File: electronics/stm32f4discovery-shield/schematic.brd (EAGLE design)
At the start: 135.6 x 110.5 mm, 41 parts, among them IC1 MAX3468CPA, IC3 LM340H-12, IC4 LM340H-12, J1 POWER_JACKSLT, Q1 BC548

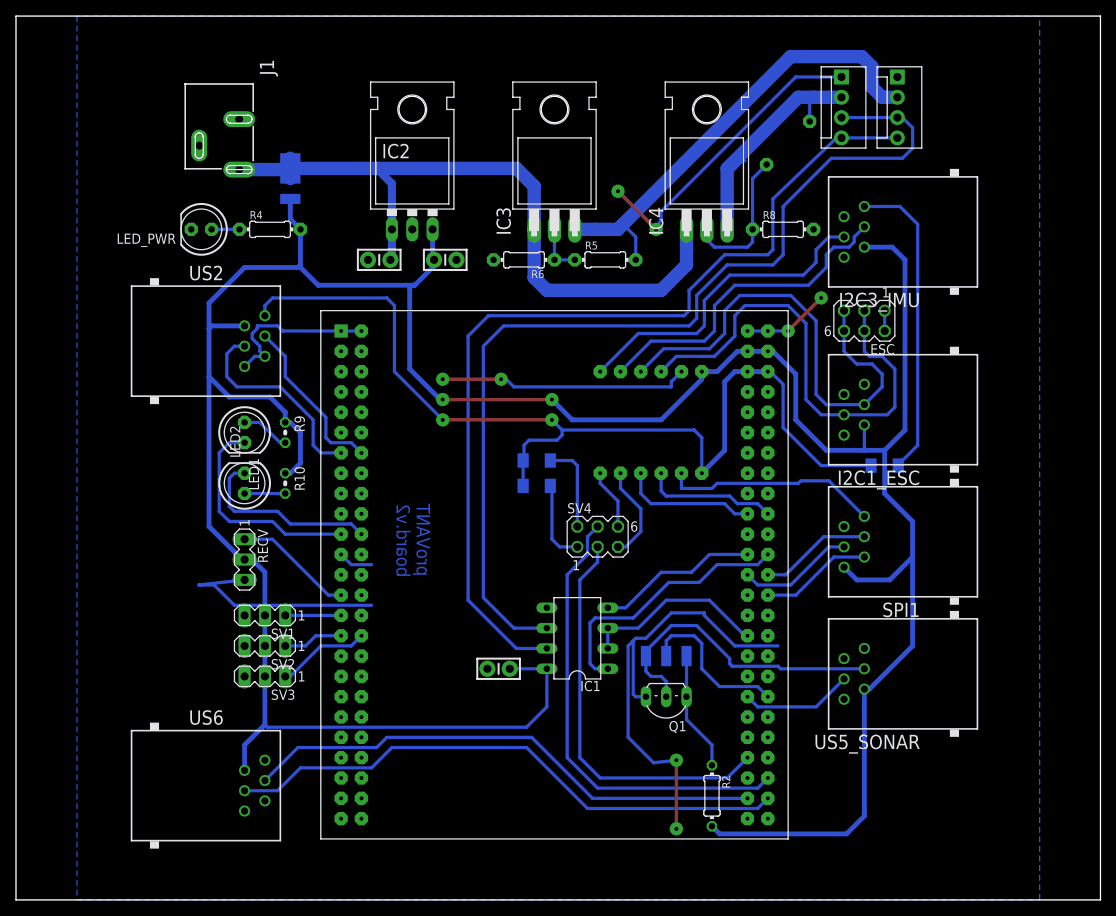
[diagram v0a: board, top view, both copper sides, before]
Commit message: Adicionado o jack para sensores analógicos. LEDs trocados para LEDs de 3mm. Verificaçao de routing do GND feita - aparentemente, sem problemas.
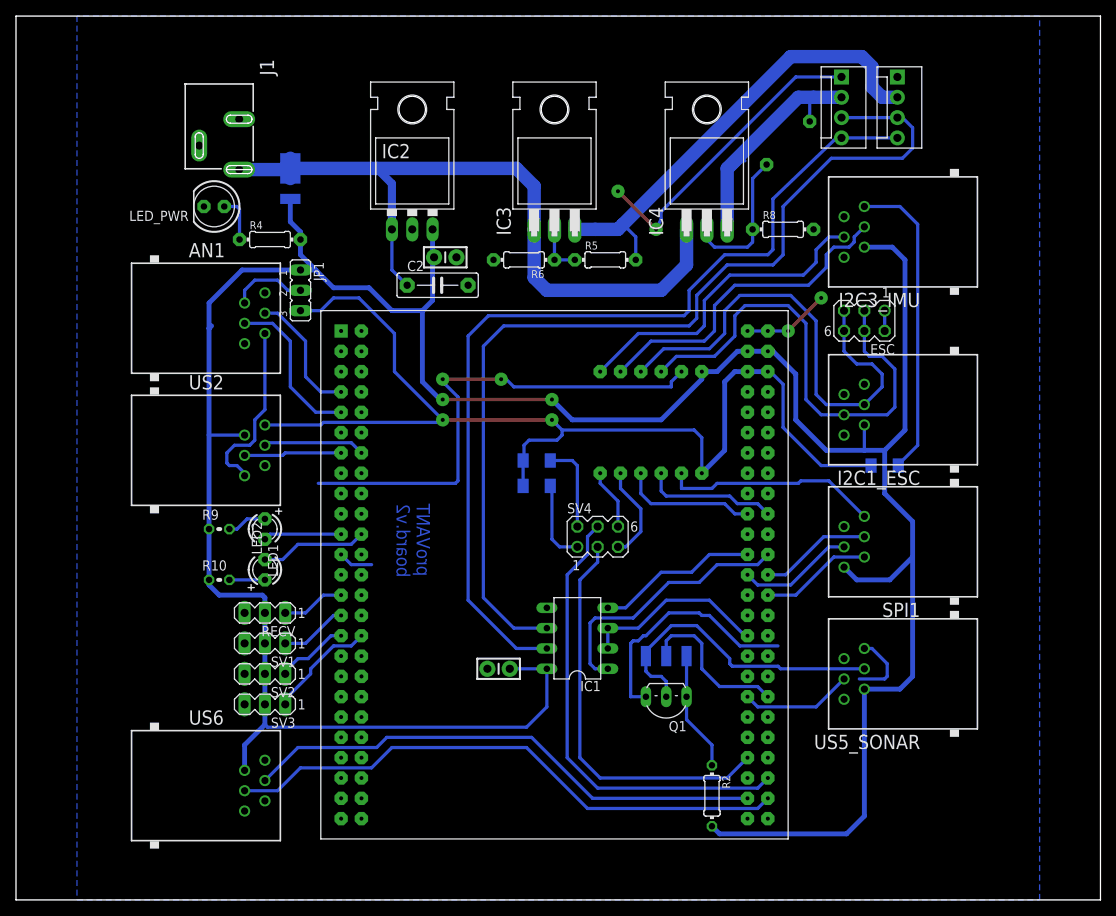
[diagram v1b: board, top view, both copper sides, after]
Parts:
- added AN1: RJ11-2L-B, con-tycoelectronics:RJ11-NO_SHIELD
- added JP1: (no value), jumper:JP2
- C2: device SparkFun-Capacitors:CAP-PTH-SMALL-KIT -> capacitor-wima:C7.5B3
- LED1, LED2: device adafruit:LED5MM -> adafruit:LED3MM
- moved R9 14.6 mm to (8.89, 46.4), turned to 0 degrees
- moved R10 14.6 mm to (8.89, 40.0), turned to 0 degrees
- moved US2 13.7 mm to (5.71, 56.2)
- moved LED1 12.3 mm to (14.6, 46.4)
- moved LED2 11.1 mm to (14.6, 41.3)
- moved C2 7.96 mm to (36.2, 76.8), turned to 0 degrees
- moved RECV 7.13 mm to (14.6, 35.9), turned to 180 degrees
- moved SV1 3.49 mm to (14.6, 32.1)
- moved SV2 3.49 mm to (14.6, 28.3)
- moved SV3 3.49 mm to (14.6, 24.4)
- moved LED_PWR 3.27 mm to (8.26, 86.7)
- moved R4 1.27 mm to (15.2, 82.5)
- moved C3 0.32 mm to (37.1, 80.3)
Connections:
- new net ADC1: AN1.3, U$1.P$7
- new net ADC3: AN1.4, U$1.P$9
- new net N$10: AN1.2, JP1.2
- net 3.3V: now also JP1.3
- net 5V: now also JP1.1
- net GND: now also AN1.5, AN1.6
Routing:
- net ADC3: track 0.00 -> 20.0 mm
- net PB1/PWM: track 27.4 -> 9.79 mm
- net ADC1: track 0.00 -> 16.2 mm
- net 3.3V: track 123.3 -> 138.3 mm
- net GND: track 222.4 -> 207.5 mm, vias 8 -> 6
- net 5V: track 380.4 -> 365.8 mm
- net PA3/USART2_RX: track 25.6 -> 12.2 mm
- net PB0/PWM: track 23.6 -> 13.4 mm
- net N$10: track 0.00 -> 9.62 mm
- net PA2/USART2_TX: track 21.1 -> 12.7 mm
- net PE9/PWM: track 15.0 -> 7.91 mm
- net VCC: track 90.7 -> 94.6 mm
- net N$4: track 3.49 -> 5.85 mm
- net PE14/PWM: track 11.6 -> 13.8 mm
- net PE13/PWM: track 7.51 -> 9.14 mm
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
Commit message: Realizado o roteamento Dual-Layer para fresamento.
Aumento de espacamento (trilhas de 24mil, espacamento 24mil)
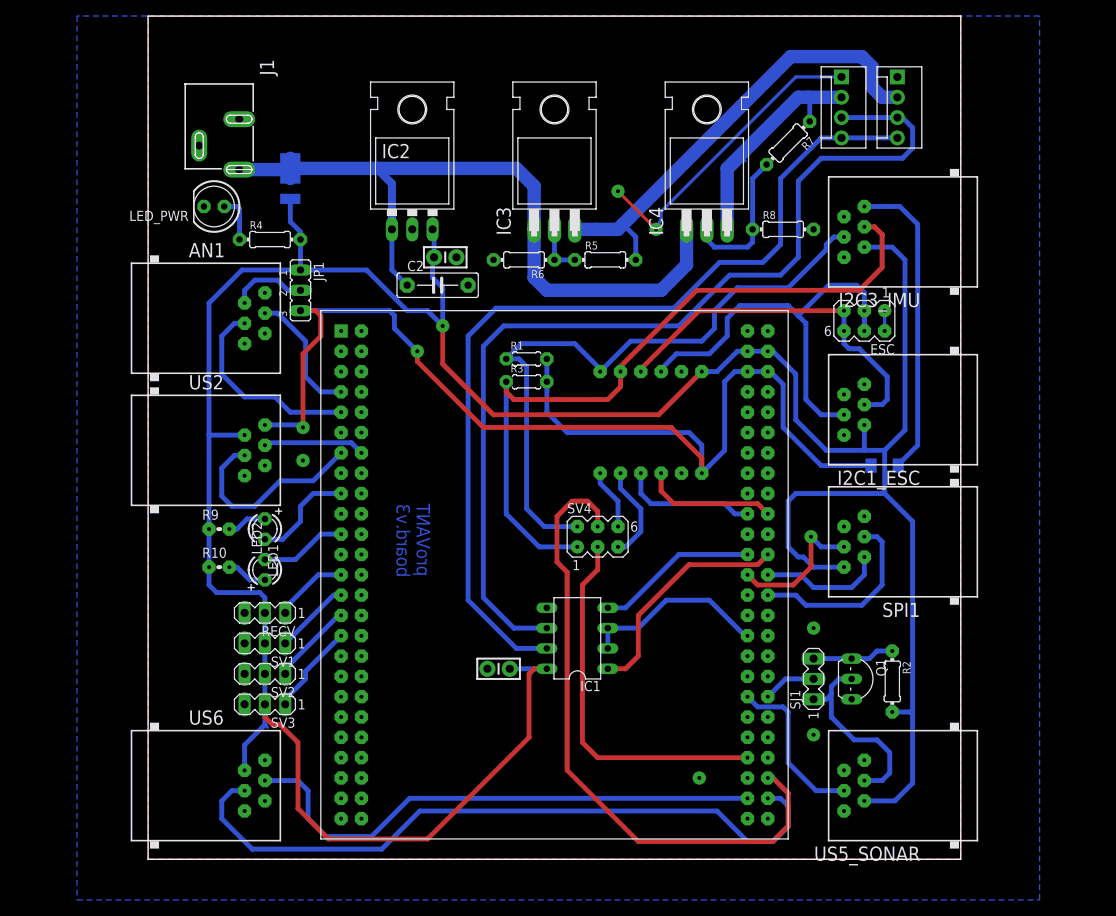
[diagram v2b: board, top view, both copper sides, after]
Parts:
- R1, R3: device adafruit:M1406 -> adafruit:0204/5
- R10, R9: device adafruit:0204V -> rcl:0204V
- SJ1: device jumper:SJ_2W -> con-lstb:MA03-1
- moved R2 26.7 mm to (93.0, 27.3)
- moved Q1 24.7 mm to (89.2, 27.6), turned to 270 degrees
- moved SJ1 18.6 mm to (83.2, 27.6), flipped to the top, turned to 90 degrees
- moved US5_SONAR 14.0 mm to (95.9, 14.3)
- moved R3 13.1 mm to (47.3, 64.8), flipped to the top
- moved R1 12.8 mm to (47.3, 67.6), flipped to the top
- moved R10 1.59 mm to (8.89, 41.6)
- flipped R7 to the top, turned to 225 degrees
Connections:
- new net PA7/PWM: LED1.K, U$1.P$17
- new net PE7: RECV.1, U$1.P$25
- net PB0/PWM: no longer LED2.K
- net PB1/PWM: now also LED2.K; no longer LED1.K
- net PB3/SPI1_SCK: now also SPI1.4; no longer SPI1.2
- net PB5/SPI1_MOSI: now also SPI1.2; no longer SPI1.4
- net PE11/PWM: now also SV2.1; no longer SV1.1
- net PE13/PWM: now also SV3.1; no longer SV2.1
- net PE14/PWM: no longer SV3.1
- net PE9/PWM: now also SV1.1; no longer RECV.1
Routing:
- net GND: track 207.5 -> 41.2 mm
- net SCL2: track 51.5 -> 90.8 mm
- net SDA2: track 52.1 -> 81.3 mm
- net PC9/I2C3_SDA: track 57.7 -> 80.1 mm
- net PC7/USART6_RX: track 71.3 -> 87.8 mm
- net 3.3V: track 138.3 -> 154.7 mm
- net SCL1: track 60.4 -> 46.0 mm
- net SONAR_RX: track 38.7 -> 24.5 mm
- net 5V: track 365.8 -> 379.7 mm, vias 2 -> 1
- net PE14/PWM: track 13.8 -> 0.00 mm
- net PB0/PWM: track 13.4 -> 0.00 mm
- net PC11/USART3_RX: track 19.9 -> 6.64 mm
- net PA3/USART2_RX: track 12.2 -> 25.2 mm
- net PA7/PWM: track 0.00 -> 13.0 mm
- net PB3/SPI1_SCK: track 14.0 -> 23.7 mm
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- added copper zone on layer 1, net GND
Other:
- board size 135.6 x 110.5 mm -> 101.6 x 105.4 mm
- board text added: "proVANT board.v3"
- board text removed: "proVANT board.v2"

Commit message: Small fixes.
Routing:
- net PC6/USART6_TX: track 67.2 -> 64.4 mm
- net ADC1: track 16.2 -> 14.0 mm
- net 5V: track 379.7 -> 377.6 mm
- net PB3/SPI1_SCK: track 23.7 -> 22.5 mm
- net SDA1: track 56.5 -> 55.3 mm
- net PB5/SPI1_MOSI: track 15.6 -> 14.3 mm
- net N$10: track 9.62 -> 8.35 mm
- net PA3/USART2_RX: track 25.2 -> 26.3 mm
- net PC7/USART6_RX: track 87.8 -> 88.8 mm
- net SCL1: track 46.0 -> 46.9 mm
- net SONAR_RX: track 24.5 -> 25.4 mm
- net 3.3V: track 154.7 -> 155.4 mm
- net PB4/SPI1_MISO: track 17.8 -> 17.3 mm
- net PA2/USART2_TX: track 12.7 -> 13.2 mm
- net SCL2: track 90.8 -> 91.4 mm
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
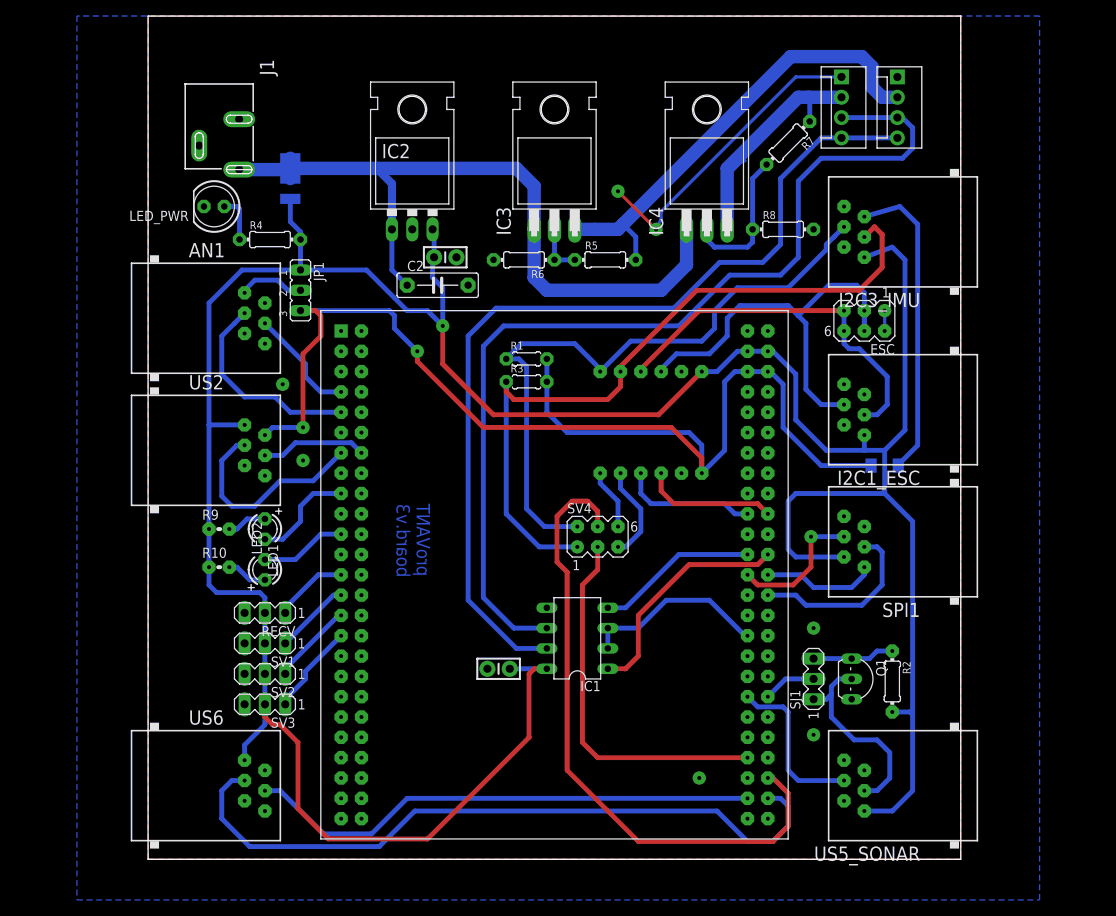
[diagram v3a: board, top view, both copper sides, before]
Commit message: Corrigido o conversor logico invertido e a pinagem incorreta de algumas portas.
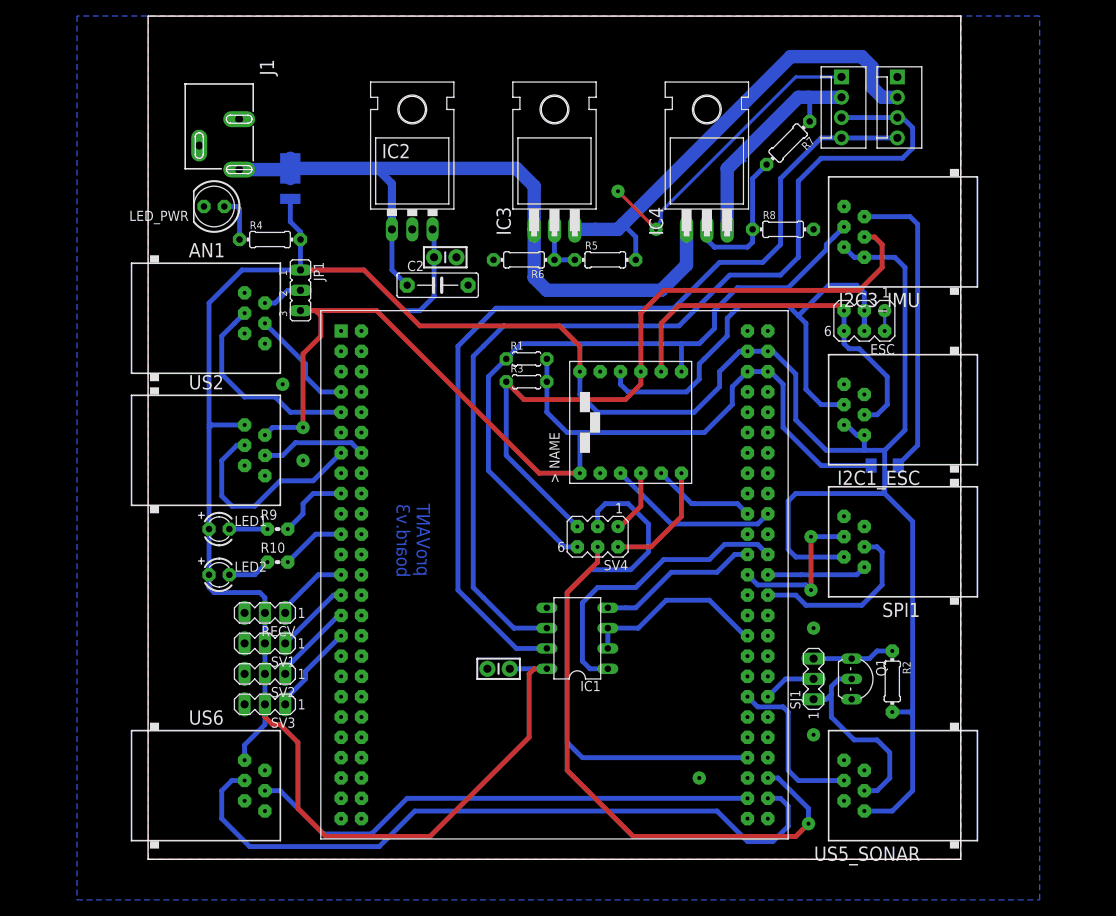
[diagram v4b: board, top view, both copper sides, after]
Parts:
- moved R10 7.33 mm to (16.2, 42.2)
- moved R9 7.30 mm to (16.2, 46.4)
- moved LED2 5.75 mm to (8.89, 40.6), turned to 0 degrees
- moved LED1 5.71 mm to (8.89, 46.4), turned to 0 degrees
- moved U$2 2.54 mm to (60.3, 59.7), flipped to the top
- turned SV4 to 180 degrees
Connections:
- net 5V: now also I2C1_ESC.1, I2C3_IMU.1, LED1.A, LED2.A; no longer R10.1, R9.1
- net N$1: now also SV4.2; no longer SV4.6
- net N$10: now also AN1.1; no longer AN1.2
- net N$2: now also SV4.1, U$2.BL; no longer SV4.5, U$2.CL
- net N$5: now also LED1.K, R9.1; no longer LED1.A, R9.2
- net N$7: now also LED2.K, R10.1; no longer LED2.A, R10.2
- net PA7/PWM: now also R9.2; no longer LED1.K
- net PB1/PWM: now also R10.2; no longer LED2.K
- net PB8/I2C1_SCL: now also U$2.CL; no longer U$2.BL
- net SCL1: now also U$2.CH; no longer U$2.BH
- net SCL2: now also SV4.5, U$2.BH; no longer SV4.1, U$2.CH
- net SDA2: now also SV4.6; no longer SV4.2
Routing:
- net 3.3V: track 155.4 -> 132.5 mm, vias 2 -> 1
- net 5V: track 377.6 -> 399.4 mm, vias 1 -> 0
- net PA8/I2C3_SCL: track 46.7 -> 67.5 mm
- net SDA1: track 55.3 -> 64.3 mm
- net PB7/USART1_RX: track 28.9 -> 37.6 mm
- net PC9/I2C3_SDA: track 80.1 -> 72.3 mm, vias 0 -> 1
- net N$1: track 7.59 -> 14.9 mm
- net PB9/I2C1_SDA: track 16.7 -> 21.6 mm
- net SCL2: track 91.4 -> 87.2 mm
- net PB8/I2C1_SCL: track 16.9 -> 12.9 mm
- net N$2: track 12.0 -> 8.04 mm
- net PA7/PWM: track 13.0 -> 9.25 mm
- net N$10: track 8.35 -> 5.10 mm
- net PB1/PWM: track 10.8 -> 8.11 mm
- net SDA2: track 81.8 -> 84.2 mm
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
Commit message: modified:   electronics/stm32f4discovery-shield/schematic.brd
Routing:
- net SCL2: track 87.2 -> 99.6 mm, vias 0 -> 1
- net N$9: track 38.2 -> 40.0 mm
- net 5V: track 399.4 -> 398.8 mm
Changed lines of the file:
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@@
 <setting verticaltext="up"/>
 </settings>
-<grid distance="0.0125" unitdist="inch" unit="inch" style="lines" multiple="1" display="yes" altdistance="0.025" altunitdist="inch" altunit="inch"/>
+<grid distance="12.5" unitdist="mil" unit="mil" style="lines" multiple="1" display="yes" altdistance="0.025" altunitdist="inch" altunit="inch"/>
 <layers>
 <layer number="1" name="Top" color="4" fill="1" visible="yes" active="yes"/>
@@
 <layer number="43" name="vRestrict" color="2" fill="10" visible="no" active="yes"/>
 <layer number="44" name="Drills" color="7" fill="1" visible="no" active="yes"/>
-<layer number="45" name="Holes" color="7" fill="1" visible="no" active="yes"/>
+<layer number="45" name="Holes" color="7" fill="1" visible="yes" active="yes"/>
 <layer number="46" name="Milling" color="3" fill="1" visible="no" active="yes"/>
 <layer number="47" name="Measures" color="7" fill="1" visible="yes" active="yes"/>
@@
 board.v3</text>
 <dimension x1="-8.89" y1="110.49" x2="111.76" y2="110.49" x3="51.435" y3="110.49" textsize="1.778" layer="48"/>
+<hole x="5" y="106" drill="3.999990625"/>
+<hole x="5" y="27" drill="3.999990625"/>
+<hole x="97" y="106" drill="3.999990625"/>
+<hole x="97" y="27" drill="3.999990625"/>
 </plain>
 <attributes>
@@
 <wire x1="8.255" y1="38.4175" x2="13.97" y2="38.4175" width="0.6096" layer="16"/>
 <wire x1="13.97" y1="38.4175" x2="14.605" y2="37.7825" width="0.6096" layer="16"/>
-<wire x1="95.5675" y1="47.3075" x2="95.5675" y2="23.1775" width="0.6096" layer="16"/>
-<wire x1="93.0275" y1="23.495" x2="95.25" y2="23.495" width="0.6096" layer="16"/>
-<wire x1="95.25" y1="23.495" x2="95.5675" y2="23.1775" width="0.6096" layer="16"/>
-<wire x1="95.5675" y1="13.6525" x2="95.5675" y2="23.1775" width="0.6096" layer="16"/>
 <wire x1="49.8475" y1="28.8925" x2="48.26" y2="28.8925" width="0.6096" layer="1"/>
 <wire x1="48.26" y1="28.8925" x2="47.625" y2="28.2575" width="0.6096" layer="1"/>
@@
 <wire x1="87.3125" y1="59.3725" x2="88.5825" y2="58.1025" width="0.6096" layer="16"/>
 <wire x1="88.5825" y1="58.1025" x2="89.535" y2="58.1025" width="0.6096" layer="16"/>
+<wire x1="93.0275" y1="23.495" x2="93.0275" y2="28.575" width="0.6096" layer="16"/>
+<wire x1="93.0275" y1="28.575" x2="95.5675" y2="31.115" width="0.6096" layer="16"/>
+<wire x1="95.5675" y1="31.115" x2="95.5675" y2="47.3075" width="0.6096" layer="16"/>
+<wire x1="95.5675" y1="13.6525" x2="95.5675" y2="19.3675" width="0.6096" layer="16"/>
+<wire x1="95.5675" y1="19.3675" x2="93.0275" y2="21.9075" width="0.6096" layer="16"/>
+<wire x1="93.0275" y1="21.9075" x2="93.0275" y2="23.495" width="0.6096" layer="16"/>
 </signal>
 <signal name="3.3V">
@@
 <contactref element="I2C3_IMU" pad="4"/>
 <contactref element="R3" pad="1"/>
-<wire x1="88.9" y1="76.2" x2="91.7575" y2="79.0575" width="0.6096" layer="1"/>
-<wire x1="89.535" y1="82.8675" x2="90.805" y2="82.8675" width="0.6096" layer="1"/>
-<wire x1="90.805" y1="82.8675" x2="91.7575" y2="81.915" width="0.6096" layer="1"/>
-<wire x1="91.7575" y1="81.915" x2="91.7575" y2="79.0575" width="0.6096" layer="1"/>
 <contactref element="U$2" pad="BH"/>
-<wire x1="88.9" y1="76.2" x2="66.9925" y2="76.2" width="0.6096" layer="1"/>
-<wire x1="66.9925" y1="76.2" x2="64.4525" y2="76.2" width="0.6096" layer="1"/>
+<wire x1="94.615" y1="76.2" x2="64.4525" y2="76.2" width="0.6096" layer="1"/>
 <wire x1="64.4525" y1="76.2" x2="61.595" y2="73.3425" width="0.6096" layer="1"/>
 <wire x1="61.595" y1="73.3425" x2="61.595" y2="66.04" width="0.6096" layer="1"/>
@@
 <wire x1="44.7675" y1="64.77" x2="44.7675" y2="55.5625" width="0.6096" layer="16"/>
 <wire x1="44.7675" y1="55.5625" x2="53.6575" y2="46.6725" width="0.6096" layer="16"/>
+<wire x1="94.615" y1="76.2" x2="96.2025" y2="74.6125" width="0.6096" layer="1"/>
+<via x="96.2025" y="74.6125" extent="1-16" drill="0.5" diameter="1.6764" shape="octagon"/>
+<wire x1="96.2025" y1="74.6125" x2="96.2025" y2="81.28" width="0.6096" layer="16"/>
+<wire x1="89.535" y1="82.8675" x2="94.615" y2="82.8675" width="0.6096" layer="16"/>
+<wire x1="94.615" y1="82.8675" x2="96.2025" y2="81.28" width="0.6096" layer="16"/>
 </signal>
 <signal name="SDA1">
@@
 <contactref element="R11" pad="2"/>
 <wire x1="93.775" y1="54.2925" x2="93.775" y2="54.405" width="0.4064" layer="16"/>
-<wire x1="93.775" y1="54.405" x2="96.2025" y2="56.8325" width="0.6096" layer="16"/>
-<wire x1="96.2025" y1="56.8325" x2="96.2025" y2="84.455" width="0.6096" layer="16"/>
-<wire x1="89.535" y1="85.4075" x2="95.25" y2="85.4075" width="0.6096" layer="16"/>
-<wire x1="95.25" y1="85.4075" x2="96.2025" y2="84.455" width="0.6096" layer="16"/>
+<wire x1="93.775" y1="54.405" x2="98.1075" y2="58.7375" width="0.6096" layer="16"/>
+<wire x1="89.535" y1="85.4075" x2="95.5675" y2="85.4075" width="0.6096" layer="16"/>
+<wire x1="95.5675" y1="85.4075" x2="98.1075" y2="82.8675" width="0.6096" layer="16"/>
+<wire x1="98.1075" y1="82.8675" x2="98.1075" y2="58.7375" width="0.6096" layer="16"/>
 </signal>
 <signal name="ADC1">
